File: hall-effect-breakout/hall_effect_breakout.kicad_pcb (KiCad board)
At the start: 2 copper layers, 12 x 22.8 mm, 3 parts, among them P1 CONN_01X04

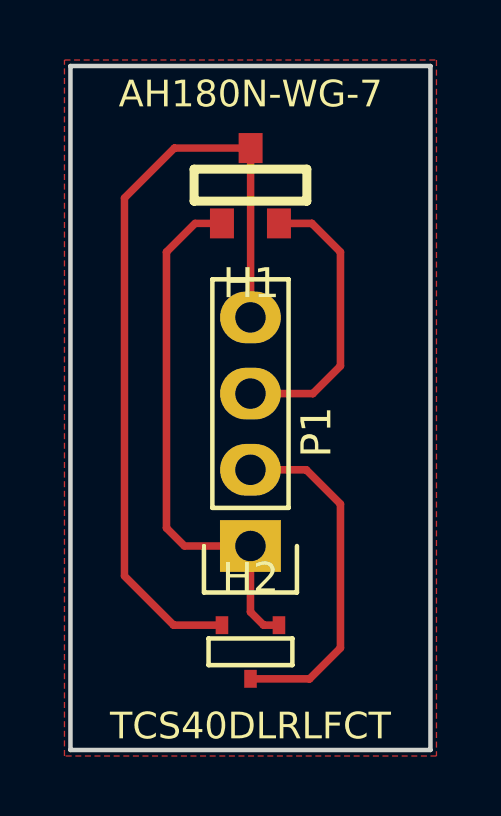
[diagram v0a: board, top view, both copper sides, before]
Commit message: Add on-copper labels
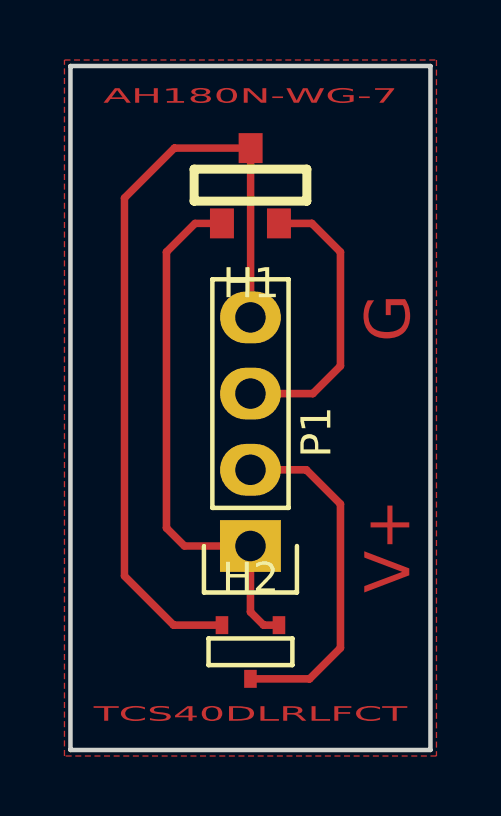
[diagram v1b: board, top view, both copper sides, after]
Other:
- board text added: "AH180N-WG-7"
- board text added: "G"
- board text added: "TCS40DLRLFCT"
- board text added: "V+"
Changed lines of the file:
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@@
     (area 129.6 92.8 142.000001 116.000001)
     (thickness 1.6)
-    (drawings 4)
+    (drawings 8)
     (tracks 25)
     (zones 0)
@@
     (visible_elements FFFFFF7F)
     (pcbplotparams
-      (layerselection 0x00030_80000001)
+      (layerselection 0x01000_80000001)
       (usegerberextensions false)
       (excludeedgelayer true)
@@
       (psnegative false)
       (psa4output false)
-      (plotreference true)
-      (plotvalue true)
+      (plotreference false)
+      (plotvalue false)
       (plotinvisibletext false)
       (padsonsilk false)
@@
       (outputformat 1)
       (mirror false)
-      (drillshape 1)
+      (drillshape 0)
       (scaleselection 1)
-      (outputdirectory ""))
+      (outputdirectory gerbers/))
   )
   (net 0 "")
@@
       (effects (font (size 1 1) (thickness 0.15)))
     )
-    (fp_text value AH180N-WG-7 (at 0.00508 -3.26644) (layer F.SilkS)
+    (fp_text value AH180N-WG-7 (at 0.00508 -3.26644) (layer F.SilkS) hide
       (effects (font (size 0.889 0.889) (thickness 0.1905)))
     )
@@
       (effects (font (size 1 1) (thickness 0.15)))
     )
-    (fp_text value TCS40DLRLFCT (at 0 -2.6 180) (layer F.SilkS)
+    (fp_text value TCS40DLRLFCT (at 0 -2.6 180) (layer F.SilkS) hide
       (effects (font (size 0.889 0.889) (thickness 0.1905)))
     )
@@
       (net 4 /TCS40-OUT))
   )
+  (gr_text V+ (at 140.4 109 90) (layer F.Cu)
+    (effects (font (size 1.5 1.5) (thickness 0.3)))
+  )
+  (gr_text G (at 140.4 101.4 90) (layer F.Cu)
+    (effects (font (size 1.5 1.5) (thickness 0.3)))
+  )
+  (gr_text AH180N-WG-7 (at 135.8 94) (layer F.Cu)
+    (effects (font (size 0.484 0.992) (thickness 0.121)))
+  )
+  (gr_text TCS40DLRLFCT (at 135.8 114.6) (layer F.Cu)
+    (effects (font (size 0.484 0.992) (thickness 0.121)))
+  )
   (gr_line (start 141.8 93) (end 129.8 93) (angle 90) (layer Edge.Cuts) (width 0.15))

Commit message: Adjust text tolerances
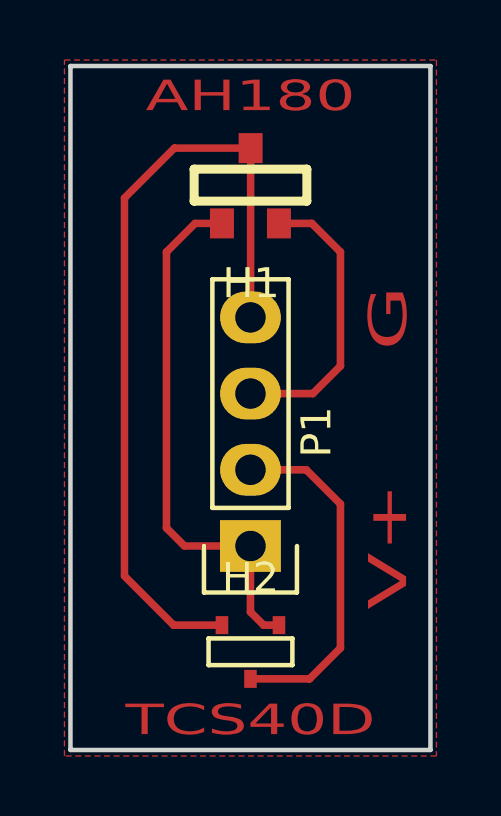
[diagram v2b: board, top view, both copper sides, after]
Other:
- board text added: "AH180"
- board text added: "TCS40D"
- board text removed: "AH180N-WG-7"
- board text removed: "TCS40DLRLFCT"
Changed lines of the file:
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@@
   )
   (gr_text V+ (at 140.4 109 90) (layer F.Cu)
-    (effects (font (size 1.5 1.5) (thickness 0.3)))
+    (effects (font (size 1.27 2.032) (thickness 0.15875)))
   )
   (gr_text G (at 140.4 101.4 90) (layer F.Cu)
-    (effects (font (size 1.5 1.5) (thickness 0.3)))
+    (effects (font (size 1.27 2.032) (thickness 0.15875)))
   )
-  (gr_text AH180N-WG-7 (at 135.8 94) (layer F.Cu)
-    (effects (font (size 0.484 0.992) (thickness 0.121)))
+  (gr_text AH180 (at 135.8 94) (layer F.Cu)
+    (effects (font (size 1.016 1.524) (thickness 0.121)))
   )
-  (gr_text TCS40DLRLFCT (at 135.8 114.6) (layer F.Cu)
-    (effects (font (size 0.484 0.992) (thickness 0.121)))
+  (gr_text TCS40D (at 135.8 114.8) (layer F.Cu)
+    (effects (font (size 1.016 1.524) (thickness 0.121)))
   )
   (gr_line (start 141.8 93) (end 129.8 93) (angle 90) (layer Edge.Cuts) (width 0.15))
